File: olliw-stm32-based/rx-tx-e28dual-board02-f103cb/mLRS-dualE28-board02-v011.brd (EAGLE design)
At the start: 39.4 x 20.3 mm, 34 parts, among them IC1 STM32F103CB, IC2 NCP1117ST33, IC3 E28-2G4M27S, IC4 74AHC1G86, IC5 74AHC1G86, IC6 E28-2G4M27S, Q1 CSTCE8M00G55-R0

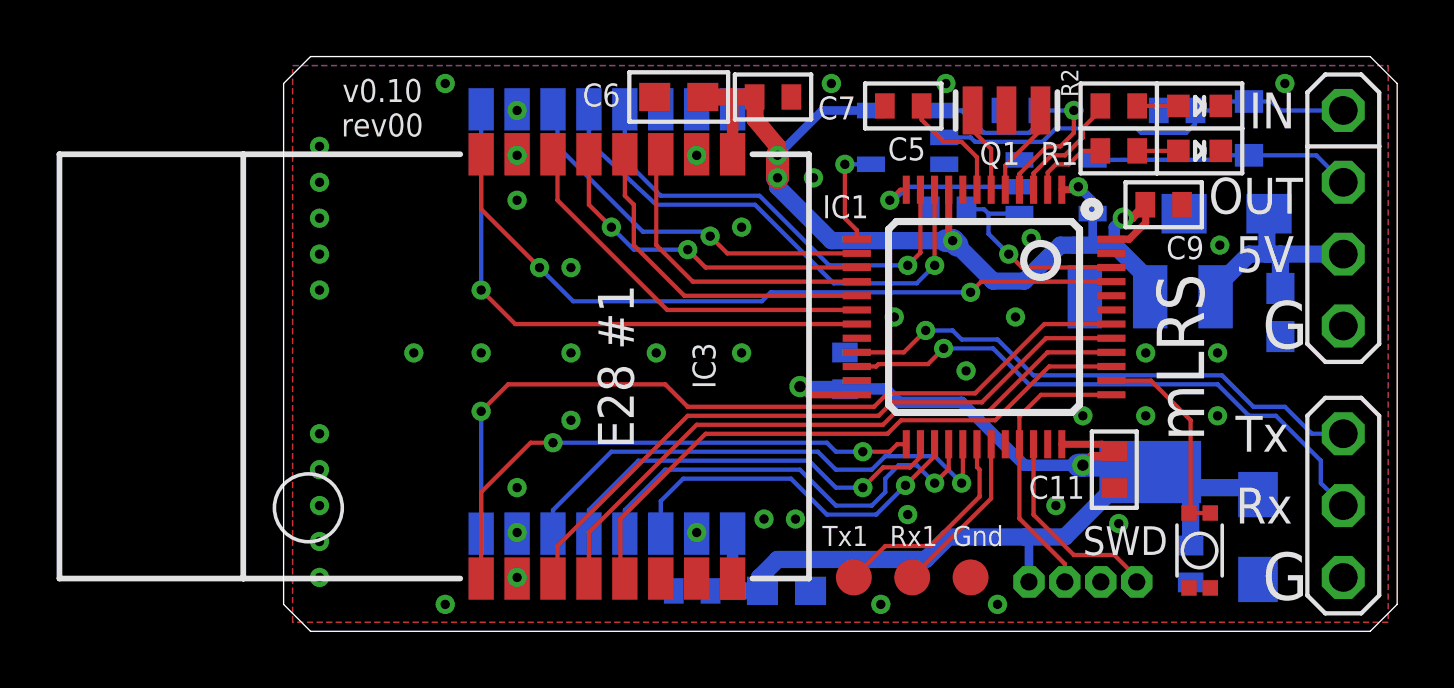
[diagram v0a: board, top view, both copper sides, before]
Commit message: rx tx module02 dualE28 F103CB v011, buzzer pad added
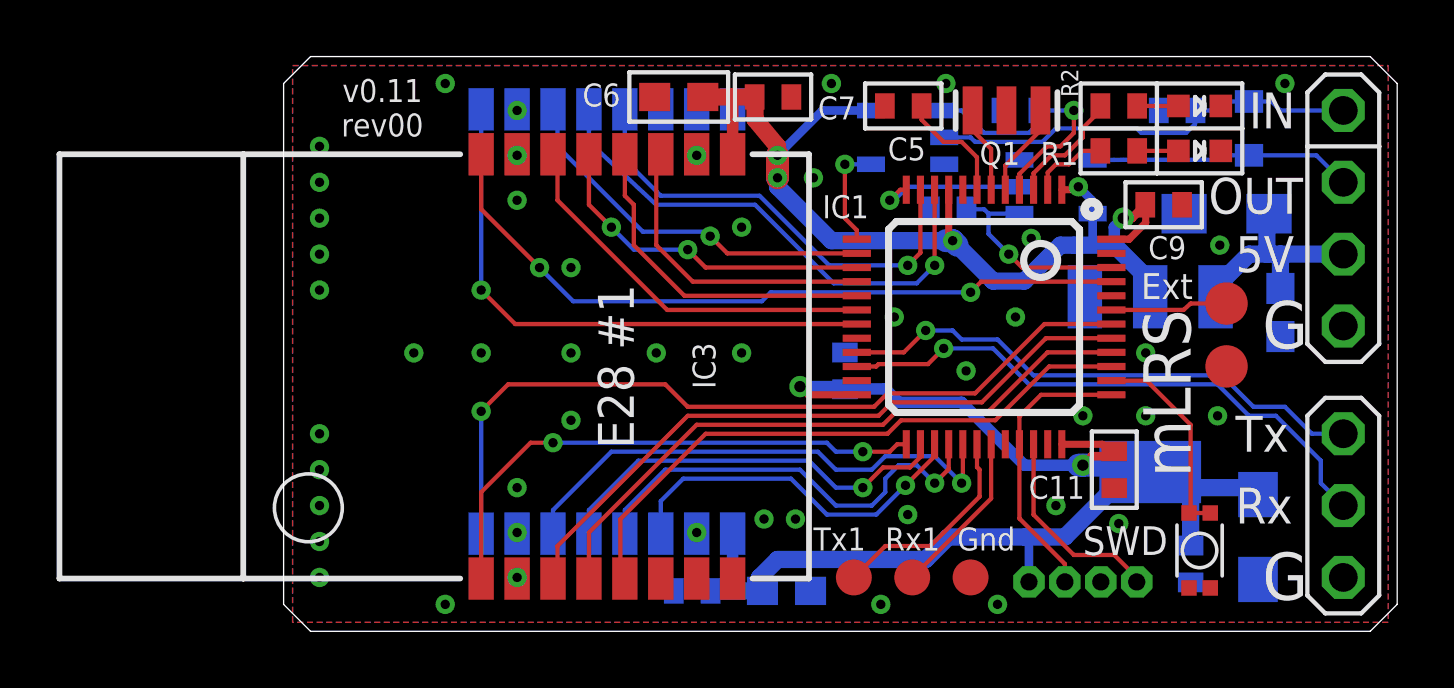
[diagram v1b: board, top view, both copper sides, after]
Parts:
- added TP4, TP5: TPTP15R, testpad:TP15R
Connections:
- new net BUZZER: IC1.43, TP4.TP
- net GND: now also TP5.TP; no longer IC1.43
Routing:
- net BUZZER: track 0.00 -> 4.16 mm
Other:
- board text added: "Ext"
- board text added: "v0.11 rev00"
- board text removed: "v0.10 rev00"
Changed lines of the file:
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@@
 <layers>
 <layer number="1" name="Top" color="4" fill="1" visible="yes" active="yes"/>
-<layer number="16" name="Bottom" color="1" fill="1" visible="yes" active="yes"/>
+<layer number="16" name="Bottom" color="1" fill="1" visible="no" active="yes"/>
 <layer number="17" name="Pads" color="2" fill="1" visible="yes" active="yes"/>
 <layer number="18" name="Vias" color="2" fill="1" visible="yes" active="yes"/>
@@
 <layer number="20" name="Dimension" color="15" fill="1" visible="yes" active="yes"/>
 <layer number="21" name="tPlace" color="7" fill="1" visible="yes" active="yes"/>
-<layer number="22" name="bPlace" color="7" fill="1" visible="yes" active="yes"/>
+<layer number="22" name="bPlace" color="7" fill="1" visible="no" active="yes"/>
 <layer number="23" name="tOrigins" color="15" fill="1" visible="yes" active="yes"/>
-<layer number="24" name="bOrigins" color="15" fill="1" visible="yes" active="yes"/>
+<layer number="24" name="bOrigins" color="15" fill="1" visible="no" active="yes"/>
 <layer number="25" name="tNames" color="7" fill="1" visible="yes" active="yes"/>
-<layer number="26" name="bNames" color="7" fill="1" visible="yes" active="yes"/>
+<layer number="26" name="bNames" color="7" fill="1" visible="no" active="yes"/>
 <layer number="27" name="tValues" color="7" fill="1" visible="no" active="yes"/>
 <layer number="28" name="bValues" color="7" fill="1" visible="no" active="yes"/>
 <layer number="29" name="tStop" color="7" fill="3" visible="yes" active="yes"/>
-<layer number="30" name="bStop" color="7" fill="6" visible="yes" active="yes"/>
+<layer number="30" name="bStop" color="7" fill="6" visible="no" active="yes"/>
 <layer number="31" name="tCream" color="7" fill="4" visible="no" active="yes"/>
 <layer number="32" name="bCream" color="7" fill="5" visible="no" active="yes"/>
 <layer number="33" name="tFinish" color="6" fill="3" visible="yes" active="yes"/>
-<layer number="34" name="bFinish" color="6" fill="6" visible="yes" active="yes"/>
+<layer number="34" name="bFinish" color="6" fill="6" visible="no" active="yes"/>
 <layer number="35" name="tGlue" color="7" fill="4" visible="no" active="yes"/>
 <layer number="36" name="bGlue" color="7" fill="5" visible="no" active="yes"/>
@@
 <layer number="38" name="bTest" color="7" fill="1" visible="no" active="yes"/>
 <layer number="39" name="tKeepout" color="4" fill="11" visible="yes" active="yes"/>
-<layer number="40" name="bKeepout" color="1" fill="11" visible="yes" active="yes"/>
+<layer number="40" name="bKeepout" color="1" fill="11" visible="no" active="yes"/>
 <layer number="41" name="tRestrict" color="4" fill="10" visible="yes" active="yes"/>
-<layer number="42" name="bRestrict" color="1" fill="10" visible="yes" active="yes"/>
+<layer number="42" name="bRestrict" color="1" fill="10" visible="no" active="yes"/>
 <layer number="43" name="vRestrict" color="2" fill="10" visible="yes" active="yes"/>
 <layer number="44" name="Drills" color="7" fill="1" visible="no" active="yes"/>
@@
 <layer number="50" name="dxf" color="7" fill="1" visible="no" active="no"/>
 <layer number="51" name="tDocu" color="7" fill="1" visible="yes" active="yes"/>
-<layer number="52" name="bDocu" color="7" fill="1" visible="yes" active="yes"/>
+<layer number="52" name="bDocu" color="7" fill="1" visible="no" active="yes"/>
 <layer number="53" name="tGND_GNDA" color="7" fill="9" visible="no" active="no"/>
 <layer number="54" name="bGND_GNDA" color="1" fill="9" visible="no" active="no"/>
@@
 <layer number="120" name="Descript" color="7" fill="1" visible="no" active="yes"/>
 <layer number="121" name="_tsilk" color="7" fill="1" visible="yes" active="yes"/>
-<layer number="122" name="_bsilk" color="7" fill="1" visible="yes" active="yes"/>
+<layer number="122" name="_bsilk" color="7" fill="1" visible="no" active="yes"/>
 <layer number="123" name="tTestmark" color="7" fill="1" visible="no" active="yes"/>
 <layer number="124" name="bTestmark" color="7" fill="1" visible="no" active="yes"/>
@@
 <text x="38.4175" y="15.08125" size="1.6764" layer="25" font="vector" ratio="15" rot="SR0">G</text>
 <text x="37.465" y="11.43" size="1.27" layer="25" font="vector" ratio="15" rot="SR0">Tx</text>
-<text x="22.86" y="8.09625" size="0.7112" layer="25" font="vector" ratio="15" rot="SR0">Tx1</text>
+<text x="22.5425" y="7.9375" size="0.8128" layer="25" font="vector" ratio="15" rot="SR0">Tx1</text>
 <wire x1="36.35375" y1="23.97125" x2="36.35375" y2="23.65375" width="0.1524" layer="25"/>
 <wire x1="36.35375" y1="23.65375" x2="36.35375" y2="23.33625" width="0.1524" layer="25"/>
@@
 <wire x1="36.35375" y1="22.06625" x2="36.03625" y2="21.74875" width="0.1524" layer="25"/>
 <wire x1="36.03625" y1="21.74875" x2="36.03625" y2="22.38375" width="0.1524" layer="25"/>
-<text x="36.35375" y="14.76375" size="1.6764" layer="25" font="vector" ratio="20" rot="SR90" align="bottom-center">mLRS</text>
-<text x="7.3025" y="24.60625" size="0.8128" layer="25" font="vector" ratio="15" rot="SR0" align="top-center">v0.10
+<text x="35.8775" y="13.49375" size="1.6764" layer="25" font="vector" ratio="20" rot="SR90" align="bottom-center">mLRS</text>
+<text x="7.3025" y="24.60625" size="0.8128" layer="25" font="vector" ratio="15" rot="SR0" align="top-center">v0.11
 rev00</text>
 <text x="36.5125" y="19.84375" size="1.27" layer="25" font="vector" ratio="15" rot="SR0">OUT</text>
@@
 <wire x1="42.545" y1="24.13" x2="41.91" y2="24.765" width="0.1524" layer="21"/>
 <wire x1="40.64" y1="24.765" x2="40.005" y2="24.13" width="0.1524" layer="21"/>
-<text x="25.24125" y="8.09625" size="0.7112" layer="25" font="vector" ratio="15" rot="SR0">Rx1</text>
-<text x="27.46375" y="8.09625" size="0.7112" layer="25" font="vector" ratio="15" rot="SR0">Gnd</text>
+<text x="25.0825" y="7.9375" size="0.8128" layer="25" font="vector" ratio="15" rot="SR0">Rx1</text>
+<text x="27.6225" y="7.9375" size="0.8128" layer="25" font="vector" ratio="15" rot="SR0">Gnd</text>
 <wire x1="34.686875" y1="24.4475" x2="31.988125" y2="24.4475" width="0.1524" layer="21"/>
 <wire x1="31.988125" y1="22.86" x2="31.988125" y2="24.4475" width="0.1524" layer="21"/>
@@
 <wire x1="22.86" y1="15.636875" x2="24.4475" y2="15.636875" width="0.1524" layer="22"/>
 <wire x1="22.86" y1="12.938125" x2="24.4475" y2="12.938125" width="0.1524" layer="22"/>
+<text x="34.13125" y="16.8275" size="0.9144" layer="25" font="vector" ratio="15" rot="SR0">Ext</text>
 </plain>
 <attributes>
@@
 </element>
 <element name="C9" library="rcl" package="C0402" value="100n" x="34.925" y="20.16125" smashed="yes">
-<attribute name="NAME" x="36.35375" y="19.05" size="0.8128" layer="25" font="vector" rot="R180"/>
+<attribute name="NAME" x="35.71875" y="19.05" size="0.8128" layer="25" font="vector" rot="R180"/>
 <attribute name="VALUE" x="35.2552" y="18.25625" size="0.8128" layer="27"/>
 </element>
@@
 </element>
 <element name="D1" library="diode" package="SOD110-R" value="1PS76SB40" x="37.94125" y="22.86" smashed="yes" rot="MR270"/>
+<element name="TP4" library="testpad" package="TP15R" value="TPTP15R" x="37.1475" y="16.66875" smashed="yes">
+<attribute name="TP_SIGNAL_NAME" value="" x="36.5125" y="14.76375" size="1" layer="37"/>
+<attribute name="VALUE" x="36.5125" y="15.90675" size="0.0254" layer="27"/>
+</element>
+<element name="TP5" library="testpad" package="TP15R" value="TPTP15R" x="37.1475" y="14.44625" smashed="yes">
+<attribute name="TP_SIGNAL_NAME" value="" x="36.5125" y="12.54125" size="1" layer="37"/>
+<attribute name="VALUE" x="36.5125" y="13.68425" size="0.0254" layer="27"/>
+</element>
 </elements>
 <signals>
@@
 <via x="34.29" y="12.7" extent="1-16" drill="0.3302"/>
 <via x="36.83" y="12.7" extent="1-16" drill="0.3302"/>
-<via x="36.83" y="14.9225" extent="1-16" drill="0.3302"/>
 <via x="34.29" y="14.9225" extent="1-16" drill="0.3302"/>
 <via x="29.68625" y="16.1925" extent="1-16" drill="0.3302"/>
@@
 <via x="8.41375" y="14.9225" extent="1-16" drill="0.3302"/>
 <via x="22.5425" y="21.11375" extent="1-16" drill="0.3302"/>
-<contactref element="IC1" pad="43"/>
 <contactref element="IC1" pad="32"/>
 <via x="27.225625" y="24.4475" extent="1-16" drill="0.3302"/>
+<contactref element="TP5" pad="TP"/>
 </signal>
 <signal name="VCC">
@@
 <wire x1="36.57" y1="9.2625" x2="35.82" y2="9.2625" width="0.1524" layer="1"/>
 <contactref element="IC1" pad="38"/>
-<wire x1="33.075" y1="13.9425" x2="34.47625" y2="13.9425" width="0.1524" layer="1"/>
-<wire x1="34.47625" y1="13.9425" x2="35.8775" y2="12.54125" width="0.1524" layer="1"/>
-<wire x1="35.8775" y1="12.54125" x2="35.8775" y2="9.36375" width="0.1524" layer="1"/>
+<wire x1="33.075" y1="13.9425" x2="34.3175" y2="13.9425" width="0.1524" layer="1"/>
+<wire x1="34.3175" y1="13.9425" x2="35.8775" y2="12.3825" width="0.1524" layer="1"/>
+<wire x1="35.8775" y1="12.3825" x2="35.8775" y2="9.36375" width="0.1524" layer="1"/>
 <wire x1="35.8775" y1="9.36375" x2="35.82" y2="9.2625" width="0.1524" layer="1"/>
 </signal>
@@
 <wire x1="27.825" y1="10.3625" x2="27.78125" y2="10.31875" width="0.1524" layer="1"/>
 </signal>
+<signal name="BUZZER">
+<contactref element="TP4" pad="TP"/>
+<contactref element="IC1" pad="43"/>
+<wire x1="33.075" y1="16.4425" x2="35.6275" y2="16.4425" width="0.1524" layer="1"/>
+<wire x1="35.6275" y1="16.4425" x2="35.8775" y2="16.66875" width="0.1524" layer="1"/>
+<wire x1="35.8775" y1="16.66875" x2="37.1475" y2="16.66875" width="0.1524" layer="1"/>
+</signal>
 </signals>
